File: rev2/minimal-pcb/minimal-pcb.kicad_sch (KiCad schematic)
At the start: 8 parts, among them J1 USB_C_Receptacle_USB2.0

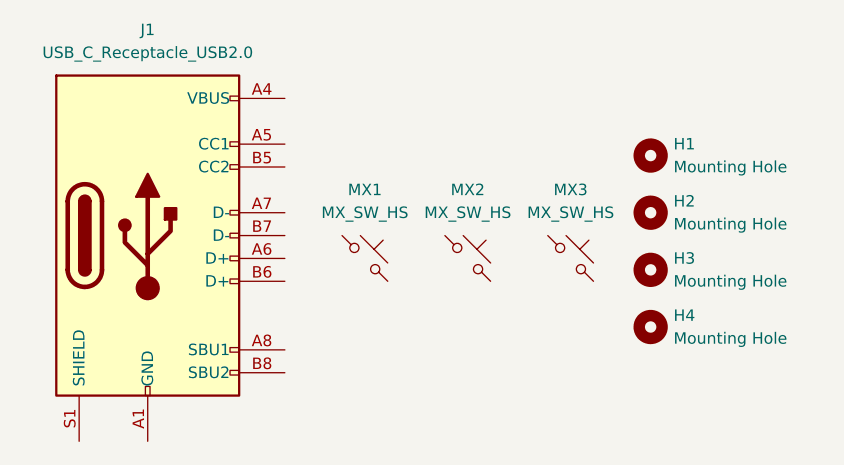
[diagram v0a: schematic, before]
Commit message: chore: update all symbols + footprints to match kicad 8
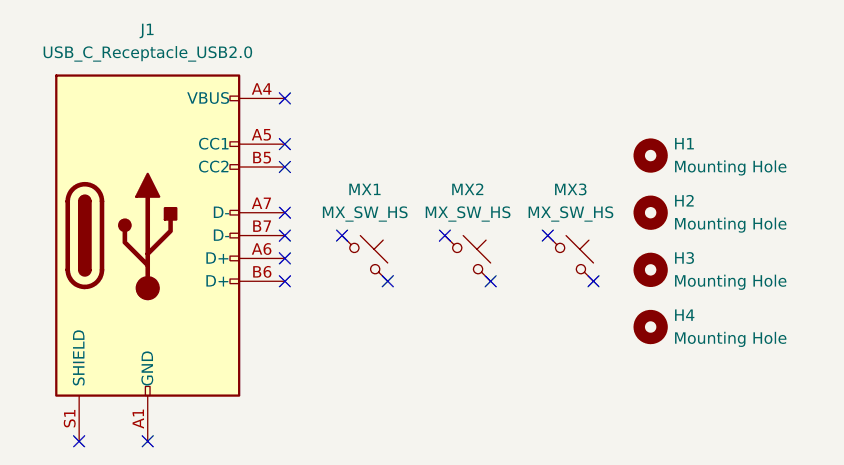
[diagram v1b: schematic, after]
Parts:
- J1: symbol Connector:USB_C_Receptacle_USB2.0 -> Connector:USB_C_Receptacle_USB2.0_14P
- MX1, MX2, MX3: footprint PCM_marbastlib-mx:SW_MX_HS_1u -> PCM_marbastlib-mx:SW_MX_HS_CPG151101S11_1u; symbol PCM_marbastlib-mx:MX_SW_HS -> PCM_marbastlib-mx:MX_SW_HS_CPG151101S11
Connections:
- no-connect marks 0 -> 15
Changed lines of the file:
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@@
 	(generator_version "8.0")
 	(paper "A4")
-	(symbol
-		(lib_id "PCM_marbastlib-mx:MX_SW_HS")
+	(no_connect
+		(at 59.69 38.1)
+	)
+	(no_connect
+		(at 76.2 43.18)
+	)
+	(no_connect
+		(at 41.91 43.18)
+	)
+	(no_connect
+		(at 41.91 40.64)
+	)
+	(no_connect
+		(at 48.26 38.1)
+	)
+	(no_connect
+		(at 53.34 43.18)
+	)
+	(no_connect
+		(at 41.91 35.56)
+	)
+	(no_connect
+		(at 41.91 22.86)
+	)
+	(no_connect
+		(at 64.77 43.18)
+	)
+	(no_connect
+		(at 41.91 38.1)
+	)
+	(no_connect
+		(at 71.12 38.1)
+	)
+	(no_connect
+		(at 19.05 60.96)
+	)
+	(no_connect
+		(at 41.91 30.48)
+	)
+	(no_connect
+		(at 26.67 60.96)
+	)
+	(no_connect
+		(at 41.91 27.94)
+	)
+	(symbol
+		(lib_id "PCM_marbastlib-mx:MX_SW_HS_CPG151101S11")
 		(at 50.8 40.64 0)
 		(unit 1)
@@
 			)
 		)
-		(property "Footprint" "PCM_marbastlib-mx:SW_MX_HS_1u"
+		(property "Footprint" "PCM_marbastlib-mx:SW_MX_HS_CPG151101S11_1u"
 			(at 50.8 40.64 0)
 			(effects
@@
 			)
 		)
-		(property "Description" ""
+		(property "Description" "Push button switch, normally open, two pins, 45° tilted, Kailh CPG151101S11 for Cherry MX style switches"
 			(at 50.8 40.64 0)
 			(effects
@@
 			)
 		)
-		(property "Description" ""
+		(property "Description" "Mounting Hole without connection"
 			(at 82.55 48.26 0)
 			(effects
@@
 			)
 		)
-		(property "Description" ""
+		(property "Description" "Mounting Hole without connection"
 			(at 82.55 41.91 0)
 			(effects
@@
 			)
 		)
-		(property "Description" ""
+		(property "Description" "Mounting Hole without connection"
 			(at 82.55 29.21 0)
 			(effects
@@
 	)
 	(symbol
-		(lib_id "Connector:USB_C_Receptacle_USB2.0")
+		(lib_id "Connector:USB_C_Receptacle_USB2.0_14P")
 		(at 26.67 38.1 0)
 		(unit 1)
@@
 			)
 		)
-		(property "Description" ""
+		(property "Description" "USB 2.0-only 14P Type-C Receptacle connector"
 			(at 26.67 38.1 0)
 			(effects
@@
 			)
 		)
-		(pin "B8"
-		)
 		(pin "A12"
 		)
@@
 		(pin "B9"
 		)
-		(pin "A8"
-		)
 		(pin "B4"
 		)
@@
 	)
 	(symbol
-		(lib_id "PCM_marbastlib-mx:MX_SW_HS")
+		(lib_id "PCM_marbastlib-mx:MX_SW_HS_CPG151101S11")
 		(at 62.23 40.64 0)
 		(unit 1)
@@
 			)
 		)
-		(property "Footprint" "PCM_marbastlib-mx:SW_MX_HS_1u"
+		(property "Footprint" "PCM_marbastlib-mx:SW_MX_HS_CPG151101S11_1u"
 			(at 62.23 40.64 0)
 			(effects
@@
 			)
 		)
-		(property "Description" ""
+		(property "Description" "Push button switch, normally open, two pins, 45° tilted, Kailh CPG151101S11 for Cherry MX style switches"
 			(at 62.23 40.64 0)
 			(effects
@@
 	)
 	(symbol
-		(lib_id "PCM_marbastlib-mx:MX_SW_HS")
+		(lib_id "PCM_marbastlib-mx:MX_SW_HS_CPG151101S11")
 		(at 73.66 40.64 0)
 		(unit 1)
@@
 			)
 		)
-		(property "Footprint" "PCM_marbastlib-mx:SW_MX_HS_1u"
+		(property "Footprint" "PCM_marbastlib-mx:SW_MX_HS_CPG151101S11_1u"
 			(at 73.66 40.64 0)
 			(effects
@@
 			)
 		)
-		(property "Description" ""
+		(property "Description" "Push button switch, normally open, two pins, 45° tilted, Kailh CPG151101S11 for Cherry MX style switches"
 			(at 73.66 40.64 0)
 			(effects
@@
 			)
 		)
-		(property "Description" ""
+		(property "Description" "Mounting Hole without connection"
 			(at 82.55 35.56 0)
 			(effects
